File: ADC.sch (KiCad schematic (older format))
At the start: 0 parts

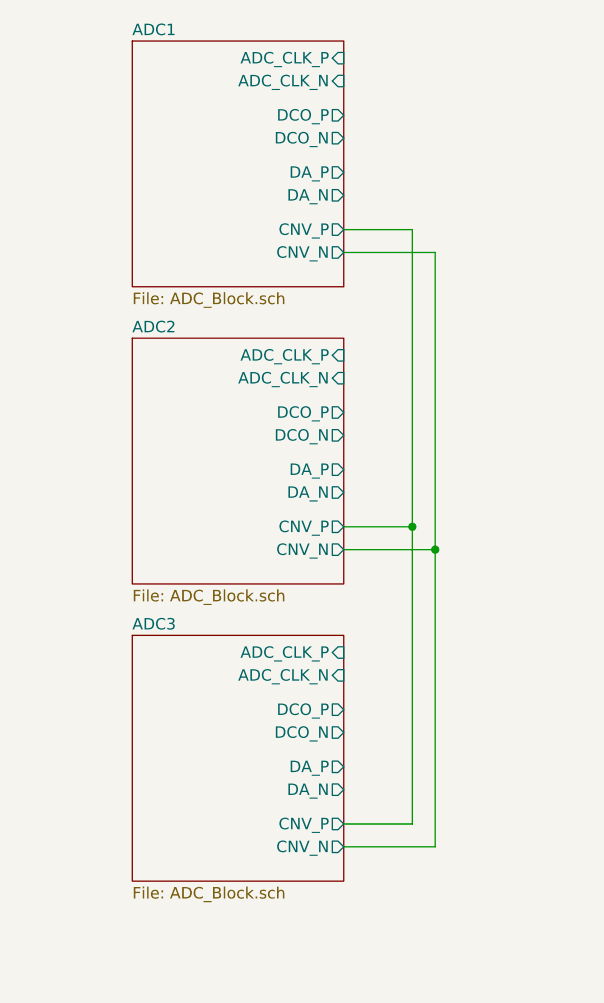
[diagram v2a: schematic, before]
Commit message: PCB created and schematics annotated High speed connections added to the BTB
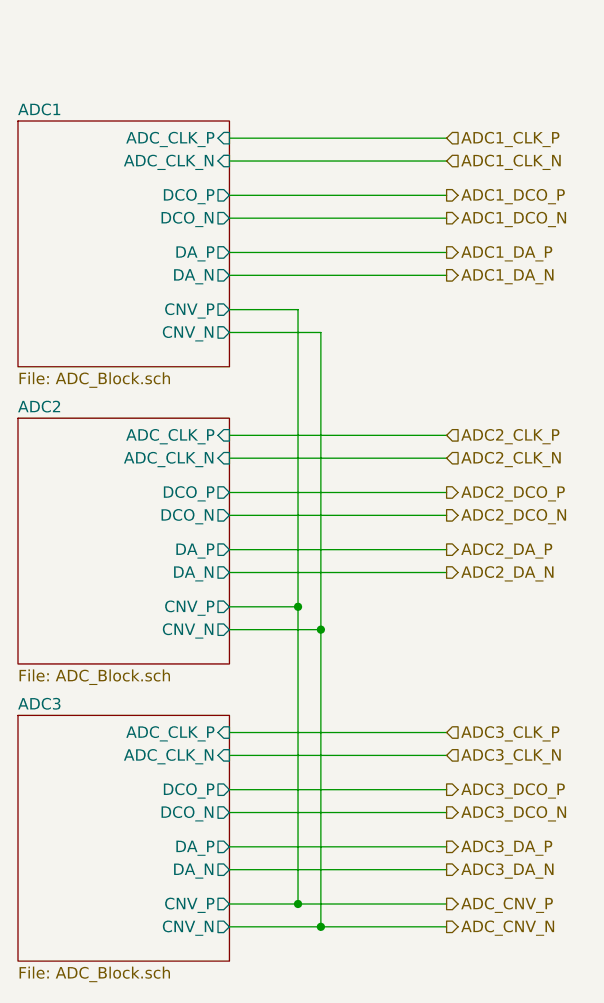
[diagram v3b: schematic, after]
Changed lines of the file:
@@
 $Descr A4 11693 8268
 encoding utf-8
-Sheet 19 25
+Sheet 17 25
 Title ""
 Date ""
@@
 $EndDescr
 $Sheet
-S 5225 1525 925  1075
+S 4725 1875 925  1075
 U 6042ACE8
 F0 "ADC1" 50
 F1 "ADC_Block.sch" 50
-F2 "ADC_CLK_P" I R 6150 1600 50
-F3 "ADC_CLK_N" I R 6150 1700 50
-F4 "DCO_P" O R 6150 1850 50
-F5 "DCO_N" O R 6150 1950 50
-F6 "DA_P" O R 6150 2100 50
-F7 "DA_N" O R 6150 2200 50
-F8 "CNV_P" O R 6150 2350 50
-F9 "CNV_N" O R 6150 2450 50
+F2 "ADC_CLK_P" I R 5650 1950 50
+F3 "ADC_CLK_N" I R 5650 2050 50
+F4 "DCO_P" O R 5650 2200 50
+F5 "DCO_N" O R 5650 2300 50
+F6 "DA_P" O R 5650 2450 50
+F7 "DA_N" O R 5650 2550 50
+F8 "CNV_P" O R 5650 2700 50
+F9 "CNV_N" O R 5650 2800 50
 $EndSheet
 $Sheet
-S 5225 2825 925  1075
+S 4725 3175 925  1075
 U 60597F99
 F0 "ADC2" 50
 F1 "ADC_Block.sch" 50
-F2 "ADC_CLK_P" I R 6150 2900 50
-F3 "ADC_CLK_N" I R 6150 3000 50
-F4 "DCO_P" O R 6150 3150 50
-F5 "DCO_N" O R 6150 3250 50
-F6 "DA_P" O R 6150 3400 50
-F7 "DA_N" O R 6150 3500 50
-F8 "CNV_P" O R 6150 3650 50
-F9 "CNV_N" O R 6150 3750 50
+F2 "ADC_CLK_P" I R 5650 3250 50
+F3 "ADC_CLK_N" I R 5650 3350 50
+F4 "DCO_P" O R 5650 3500 50
+F5 "DCO_N" O R 5650 3600 50
+F6 "DA_P" O R 5650 3750 50
+F7 "DA_N" O R 5650 3850 50
+F8 "CNV_P" O R 5650 4000 50
+F9 "CNV_N" O R 5650 4100 50
 $EndSheet
 $Sheet
-S 5225 4125 925  1075
+S 4725 4475 925  1075
 U 605990AC
 F0 "ADC3" 50
 F1 "ADC_Block.sch" 50
-F2 "ADC_CLK_P" I R 6150 4200 50
-F3 "ADC_CLK_N" I R 6150 4300 50
-F4 "DCO_P" O R 6150 4450 50
-F5 "DCO_N" O R 6150 4550 50
-F6 "DA_P" O R 6150 4700 50
-F7 "DA_N" O R 6150 4800 50
-F8 "CNV_P" O R 6150 4950 50
-F9 "CNV_N" O R 6150 5050 50
+F2 "ADC_CLK_P" I R 5650 4550 50
+F3 "ADC_CLK_N" I R 5650 4650 50
+F4 "DCO_P" O R 5650 4800 50
+F5 "DCO_N" O R 5650 4900 50
+F6 "DA_P" O R 5650 5050 50
+F7 "DA_N" O R 5650 5150 50
+F8 "CNV_P" O R 5650 5300 50
+F9 "CNV_N" O R 5650 5400 50
 $EndSheet
 Wire Wire Line
-	6150 2350 6450 2350
+	5650 2700 5950 2700
 Wire Wire Line
-	6450 2350 6450 3650
+	5950 2700 5950 4000
 Wire Wire Line
-	6450 3650 6150 3650
+	5950 4000 5650 4000
 Wire Wire Line
-	6450 3650 6450 4950
+	5950 4000 5950 5300
 Wire Wire Line
-	6450 4950 6150 4950
-Connection ~ 6450 3650
+	5950 5300 5650 5300
+Connection ~ 5950 4000
 Wire Wire Line
-	6150 5050 6550 5050
+	5650 5400 6050 5400
 Wire Wire Line
-	6550 5050 6550 3750
+	6050 5400 6050 4100
 Wire Wire Line
-	6550 3750 6150 3750
+	6050 4100 5650 4100
 Wire Wire Line
-	6550 2450 6150 2450
+	6050 2800 5650 2800
 Wire Wire Line
-	6550 2450 6550 3750
-Connection ~ 6550 3750
+	6050 2800 6050 4100
+Connection ~ 6050 4100
+Text HLabel 6600 1950 2    50   Input ~ 0
+ADC1_CLK_P
+Text HLabel 6600 2050 2    50   Input ~ 0
+ADC1_CLK_N
+Text HLabel 6600 2200 2    50   Output ~ 0
+ADC1_DCO_P
+Text HLabel 6600 2300 2    50   Output ~ 0
+ADC1_DCO_N
+Text HLabel 6600 2450 2    50   Output ~ 0
+ADC1_DA_P
+Text HLabel 6600 2550 2    50   Output ~ 0
+ADC1_DA_N
+Wire Wire Line
+	5650 1950 6600 1950
+Wire Wire Line
+	6600 2050 5650 2050
+Wire Wire Line
+	5650 2200 6600 2200
+Wire Wire Line
+	6600 2300 5650 2300
+Wire Wire Line
+	6600 2450 5650 2450
+Wire Wire Line
+	6600 2550 5650 2550
+Text HLabel 6600 3250 2    50   Input ~ 0
+ADC2_CLK_P
+Text HLabel 6600 3350 2    50   Input ~ 0
+ADC2_CLK_N
+Text HLabel 6600 3500 2    50   Output ~ 0
+ADC2_DCO_P
+Text HLabel 6600 3600 2    50   Output ~ 0
+ADC2_DCO_N
+Text HLabel 6600 3750 2    50   Output ~ 0
+ADC2_DA_P
+Text HLabel 6600 3850 2    50   Output ~ 0
+ADC2_DA_N
+Wire Wire Line
+	5650 3250 6600 3250
+Wire Wire Line
+	6600 3350 5650 3350
+Wire Wire Line
+	5650 3500 6600 3500
+Wire Wire Line
+	6600 3600 5650 3600
+Wire Wire Line
+	6600 3750 5650 3750
+Wire Wire Line
+	6600 3850 5650 3850
+Text HLabel 6600 4550 2    50   Input ~ 0
+ADC3_CLK_P
+Text HLabel 6600 4650 2    50   Input ~ 0
+ADC3_CLK_N
+Text HLabel 6600 4800 2    50   Output ~ 0
+ADC3_DCO_P
+Text HLabel 6600 4900 2    50   Output ~ 0
+ADC3_DCO_N
+Text HLabel 6600 5050 2    50   Output ~ 0
+ADC3_DA_P
+Text HLabel 6600 5150 2    50   Output ~ 0
+ADC3_DA_N
+Wire Wire Line
+	5650 4550 6600 4550
+Wire Wire Line
+	6600 4650 5650 4650
+Wire Wire Line
+	5650 4800 6600 4800
+Wire Wire Line
+	6600 4900 5650 4900
+Wire Wire Line
+	6600 5050 5650 5050
+Wire Wire Line
+	6600 5150 5650 5150
+Text HLabel 6600 5300 2    50   Output ~ 0
+ADC_CNV_P
+Text HLabel 6600 5400 2    50   Output ~ 0
+ADC_CNV_N
+Wire Wire Line
+	5950 5300 6600 5300
+Connection ~ 5950 5300
+Wire Wire Line
+	6600 5400 6050 5400
+Connection ~ 6050 5400
 $EndSCHEMATC
